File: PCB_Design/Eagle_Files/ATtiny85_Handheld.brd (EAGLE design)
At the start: 86.3 x 63.2 mm, 21 parts

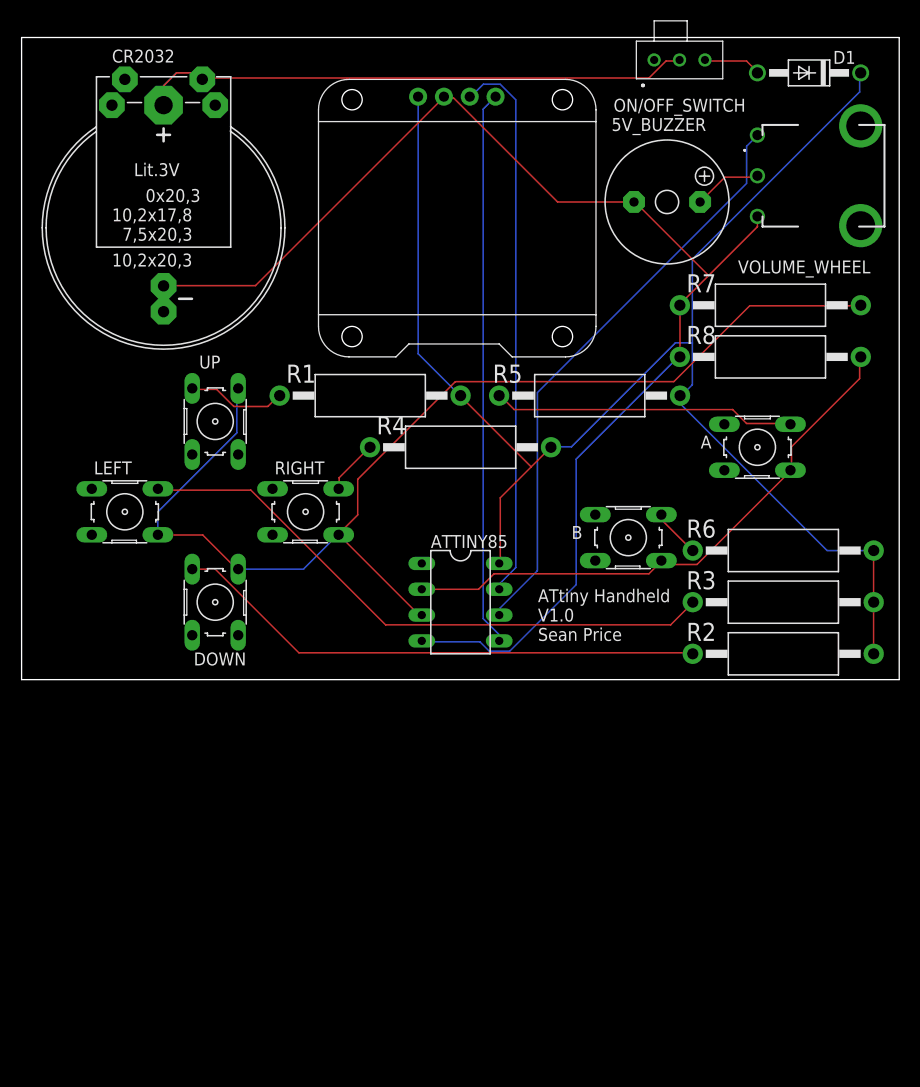
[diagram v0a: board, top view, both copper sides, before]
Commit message: V1.2.0 Updated the PCB to V1.1
- Option of using silicone or tactile buttons
- Removed D1
- Hand-router, thicker traces
- Broke the schematic into sections to make it easier to follow
- Update/fixed the battery holder footprint
- Changed the switch footprint to use an angled slide switch
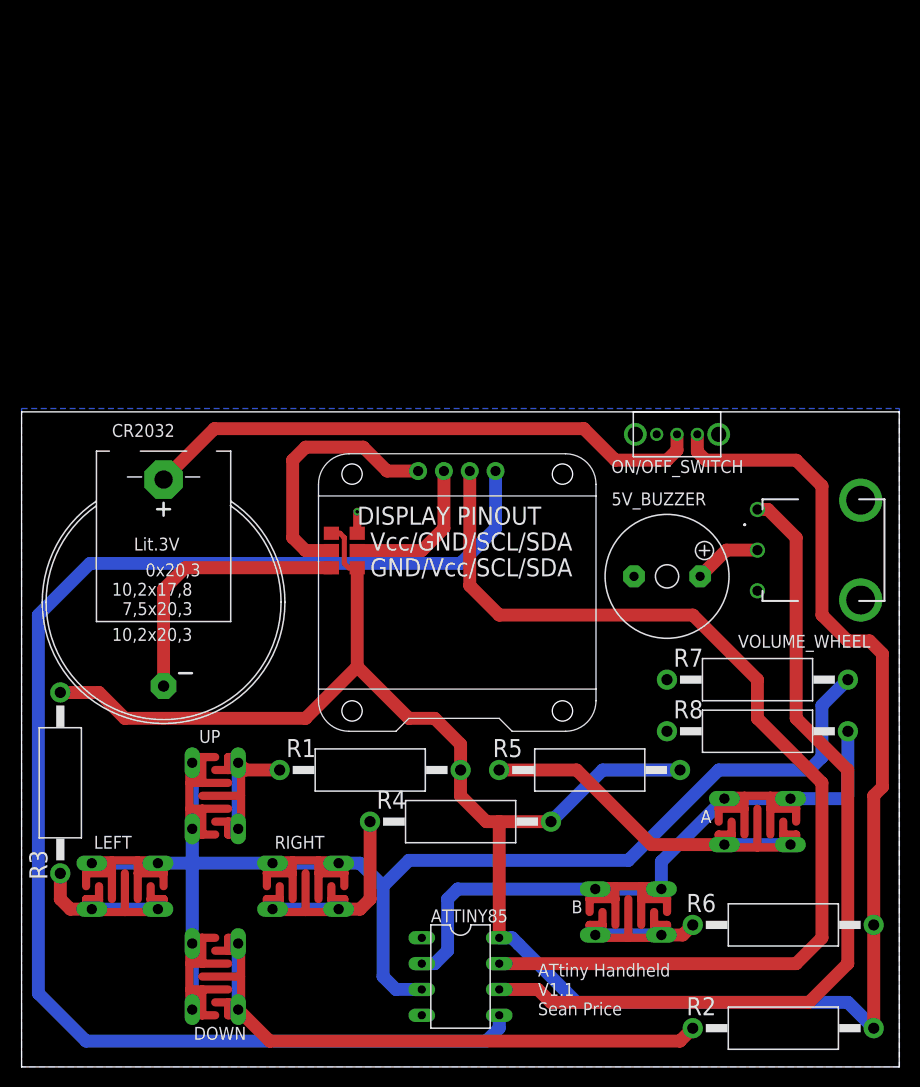
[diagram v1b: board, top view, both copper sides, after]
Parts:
- removed D1: 1N4004, diode:DO41-10
- added JMP1, JMP2: 0R-JUMPA, jump-0r-smd:A0R-JMP
- A, B, DOWN, LEFT, RIGHT, UP: value (none) -> TACTILE/SILICONE_BUTTON; device switch-omron:B3F-10XX -> Tactile_&_SIlicone_Button:TACTILE/SILICONE_BUTTON
- CR2032: value B2430UNI -> CR2032_BATTERY_HOLDER; device battery:B2430UNI -> CR2032_Battery_Holder:CR2032_BATTERY_HOLDER
- ON/OFF_SWITCH: value COM-09609 -> OS102011MA1QN1; device COM-09609:COM09609 -> OS102011MA1QN1:OS102011MA1QN1
- moved R3 73.3 mm to (3.81, 26.7), turned to 90 degrees
- moved ON/OFF_SWITCH 36.9 mm to (64.5, 61.0), turned to 180 degrees
- moved R7 36.9 mm to (72.4, 36.8)
- moved R8 36.9 mm to (72.4, 31.8)
- moved ATTINY85 36.8 mm to (43.2, 7.62)
- moved DOWN 36.8 mm to (19.1, 7.62)
- moved VOLUME_WHEEL 36.8 mm to (72.4, 52.1)
- moved A 36.8 mm to (72.4, 22.9)
- moved B 36.8 mm to (59.7, 14.0)
- moved CR2032 36.8 mm to (14.0, 44.5)
- moved LEFT 36.8 mm to (10.2, 16.5)
- moved R1 36.8 mm to (34.3, 27.9)
- moved R2 36.8 mm to (74.9, 2.54)
- moved R4 36.8 mm to (43.2, 22.9)
- moved R5 36.8 mm to (55.9, 27.9)
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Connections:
- net N$12 renamed SDA
- net N$13 renamed SCL
- net N$15 renamed PWM
- removed net N$10: A.4, ATTINY85.2, B.4, R8.2
- removed net N$11: 5V_BUZZER.-, ATTINY85.4, CR2032.-, R7.1, R8.1, U$1.GND, VOLUME_WHEEL.3
- removed net N$16: D1.A, ON/OFF_SWITCH.3
- removed net N$2: ATTINY85.8, D1.C, R1.2, R2.2, R3.2, R4.2, R5.2, R6.2, U$1.VCC
- removed net N$7: ATTINY85.3, DOWN.4, LEFT.4, R7.2, RIGHT.4, UP.4
- new net A2: ATTINY85.3, DOWN.1, DOWN.2, LEFT.1, LEFT.2, R7.2, RIGHT.1, RIGHT.2, UP.1, UP.2
- new net A3: A.1, A.2, ATTINY85.2, B.1, B.2, R8.2
- new net DISP_1: JMP1.2, U$1.VCC
- new net DISP_2: JMP2.2, U$1.GND
- new net GND: 5V_BUZZER.-, ATTINY85.4, CR2032.-@1, JMP1.3, JMP2.1, R7.1, R8.1, VOLUME_WHEEL.3
- new net VCC: ATTINY85.8, JMP1.1, JMP2.3, ON/OFF_SWITCH.1, R1.2, R2.2, R3.2, R4.2, R5.2, R6.2
- net N$1: now also CR2032.+@4; no longer CR2032.+
- net N$3: now also RIGHT.3, RIGHT.4; no longer RIGHT.2
- net N$4: now also LEFT.3, LEFT.4; no longer LEFT.2
- net N$5: now also DOWN.3, DOWN.4; no longer DOWN.2
- net N$6: now also UP.3, UP.4; no longer UP.2
- net N$8: now also A.3, A.4; no longer A.2
- net N$9: now also B.3, B.4; no longer B.2
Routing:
- net VCC: track 0.00 -> 215.6 mm
- net N$2: track 148.0 -> 0.00 mm
- net N$11: track 130.7 -> 0.00 mm
- net A2: track 0.00 -> 124.5 mm
- net N$7: track 112.7 -> 0.00 mm
- net SDA: track 54.7 -> 140.4 mm
- net A3: track 0.00 -> 59.7 mm
- net N$10: track 55.6 -> 0.00 mm
- net SCL: track 54.6 -> 104.2 mm
- net N$4: track 59.2 -> 12.5 mm
- net GND: track 0.00 -> 29.0 mm, vias 0 -> 1
- net PWM: track 57.7 -> 85.4 mm
- net DISP_1: track 0.00 -> 25.8 mm
- net DISP_2: track 0.00 -> 15.1 mm
- net N$3: track 5.39 -> 17.6 mm
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- added copper zone on layer 16, net GND
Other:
- board size 86.3 x 63.2 mm -> 86.3 x 64.4 mm
- board text added: "ATtiny Handheld V1.1 Sean Price"
- board text added: "DISPLAY PINOUT"
- board text added: "GND/Vcc/SCL/SDA"
- board text added: "Vcc/GND/SCL/SDA"
- board text removed: "ATtiny Handheld V1.0 Sean Price"

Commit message: V1.2.1 Finalised PCB V1.1
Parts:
- moved R7 1.27 mm to (72.4, 38.1)
- moved R8 1.27 mm to (72.4, 33.0)
- moved U$1 1.27 mm to (43.2, 47.0)
- moved UP 1.27 mm to (19.1, 26.7)
- moved VOLUME_WHEEL 1.27 mm to (72.4, 53.3)
- moved R6 1.27 mm to (74.9, 14.0)
- moved ATTINY85 1.27 mm to (43.2, 8.89)
- moved DOWN 1.27 mm to (19.1, 8.89)
- moved R2 1.27 mm to (74.9, 3.81)
- moved A 1.27 mm to (72.4, 24.1)
- moved B 1.27 mm to (59.7, 15.2)
- moved LEFT 1.27 mm to (10.2, 17.8)
- moved R1 1.27 mm to (34.3, 29.2)
- moved R3 1.27 mm to (3.81, 27.9)
- moved R4 1.27 mm to (43.2, 24.1)
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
